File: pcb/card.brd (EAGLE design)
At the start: 69.5 x 40.6 mm, 24 parts, among them IC1 74HC14D, IC2 24LC256SN, Q1 BC817

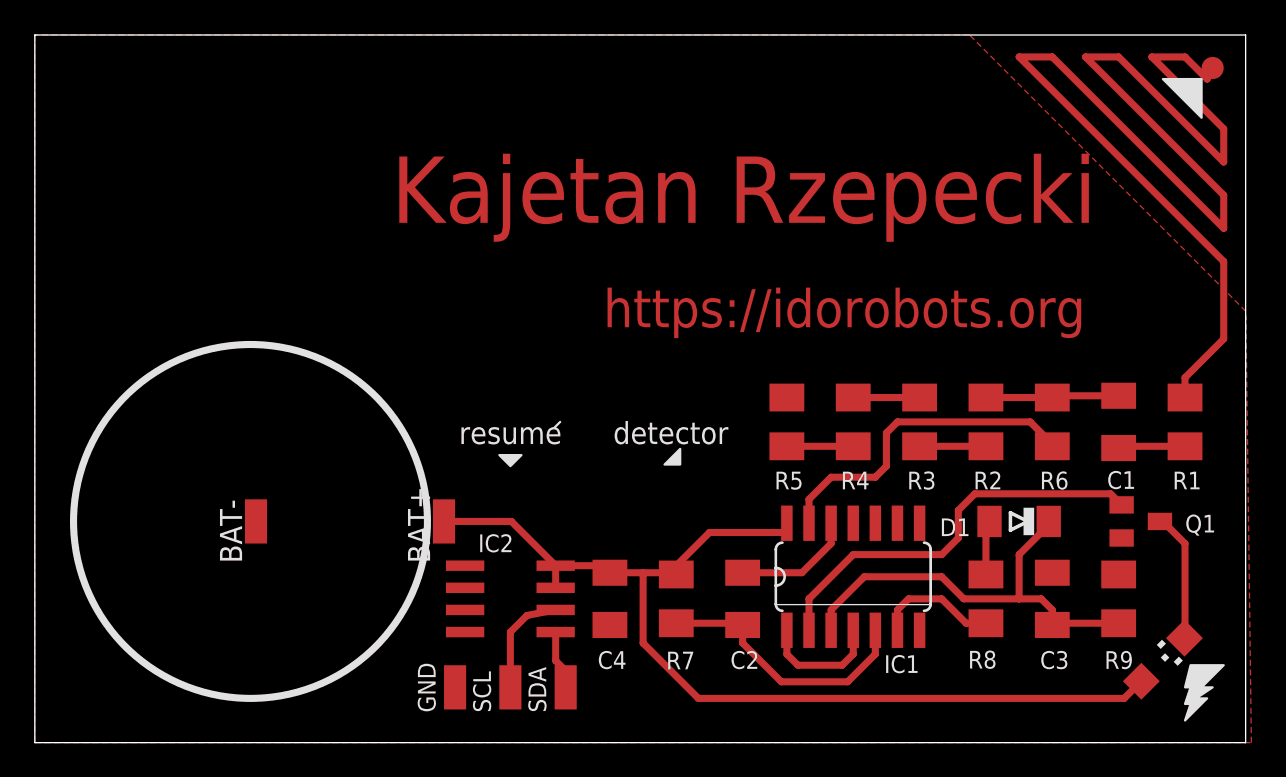
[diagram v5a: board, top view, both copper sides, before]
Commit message: Added the battery holder to the schematic.
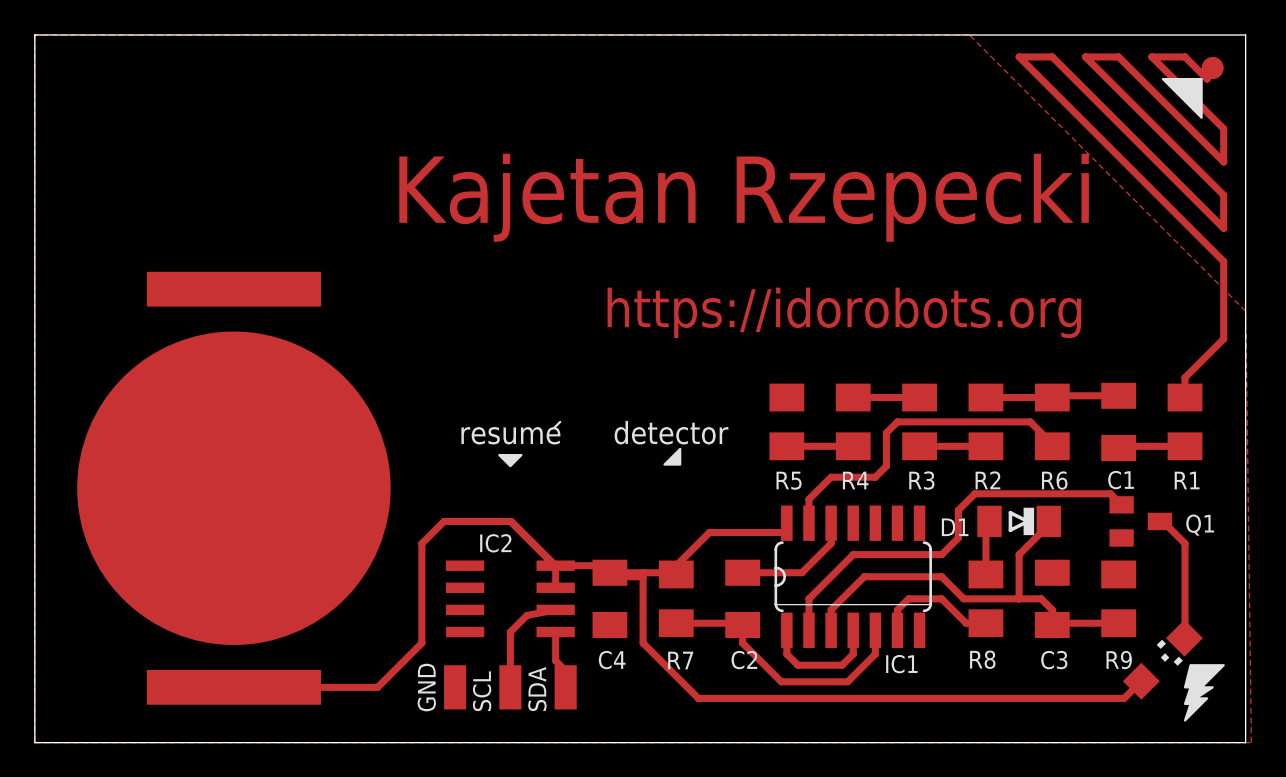
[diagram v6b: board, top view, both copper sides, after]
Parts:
- removed BAT+, BAT-: (no value), wirepad:SMD1,27-2,54
- added BAT: KB3003, bat:KB3003
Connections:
- net GND: now also BAT.-; no longer BAT-.1
- net VCC: now also BAT.+@1, BAT.+@2; no longer BAT+.1
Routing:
- net VCC: track 58.9 -> 85.1 mm
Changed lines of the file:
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@@
 <text x="60.96" y="33.655" size="3.81" layer="1" rot="R180">Kajetan Rzepecki</text>
 <text x="60.325" y="26.035" size="2.1844" layer="1" rot="R180">https://idorobots.org</text>
-<circle x="12.3825" y="12.7" radius="10.16" width="0.4064" layer="25"/>
 <text x="60.96" y="33.655" size="3.81" layer="29" rot="R180">Kajetan Rzepecki</text>
 <text x="60.325" y="26.035" size="2.1844" layer="29" rot="R180">https://idorobots.org</text>
@@
 <attribute name="NAME" x="26.1875" y="1.7275" size="1.016" layer="25" rot="R90"/>
 </element>
-<element name="BAT+" library="wirepad" package="SMD1,27-2,54" value="" x="23.495" y="12.7"/>
-<element name="BAT-" library="wirepad" package="SMD1,27-2,54" value="" x="12.7" y="12.7"/>
 <element name="IC2" library="microchip" package="SO-08" value="24LC256SN" x="27.305" y="8.255" smashed="yes" rot="R270">
 <attribute name="OC_FARNELL" value="9757996" x="27.305" y="8.255" size="1.016" layer="27" rot="R270" display="off"/>
@@
 <attribute name="VALUE" x="66.9925" y="37.973" size="0.0254" layer="27"/>
 </element>
+<element name="BAT" library="bat" package="KB3003" value="KB3003" x="11.43" y="14.605" rot="R90"/>
 </elements>
 <signals>
@@
 <vertex x="53.6575" y="40.64"/>
 </polygon>
-<contactref element="BAT-" pad="1"/>
 <contactref element="IC2" pad="1"/>
 <contactref element="IC2" pad="2"/>
@@
 <contactref element="GND" pad="1"/>
 <contactref element="R5" pad="1"/>
+<contactref element="BAT" pad="-"/>
 </signal>
 <signal name="VCC">
@@
 <contactref element="LED" pad="A"/>
 <contactref element="C4" pad="2"/>
-<contactref element="BAT+" pad="1"/>
 <contactref element="IC2" pad="8"/>
 <contactref element="IC2" pad="7"/>
@@
 <wire x1="38.735" y1="12.065" x2="43.18" y2="12.065" width="0.4064" layer="1"/>
 <wire x1="43.18" y1="12.065" x2="43.18" y2="12.5984" width="0.4064" layer="1"/>
-<wire x1="38.1" y1="2.54" x2="34.925" y2="5.715" width="0.4064" layer="1"/>
-<wire x1="34.925" y1="5.715" x2="34.925" y2="9.755" width="0.4064" layer="1"/>
+<wire x1="34.925" y1="9.525" x2="34.925" y2="9.755" width="0.4064" layer="1"/>
 <wire x1="29.905" y1="10.16" x2="29.905" y2="8.89" width="0.4064" layer="1"/>
 <wire x1="33.2775" y1="10.0125" x2="33.02" y2="9.755" width="0.4064" layer="1"/>
-<wire x1="23.495" y1="12.7" x2="27.365" y2="12.7" width="0.4064" layer="1"/>
 <wire x1="27.365" y1="12.7" x2="29.905" y2="10.16" width="0.4064" layer="1"/>
-<wire x1="29.905" y1="10.16" x2="32.9325" y2="10.16" width="0.4064" layer="1"/>
+<wire x1="29.905" y1="10.16" x2="32.385" y2="10.16" width="0.4064" layer="1"/>
+<wire x1="32.385" y1="10.16" x2="32.9325" y2="10.16" width="0.4064" layer="1"/>
 <wire x1="32.9325" y1="10.16" x2="33.02" y2="9.755" width="0.4064" layer="1"/>
+<contactref element="BAT" pad="+@2" route="any" routetag="G$1.+"/>
+<contactref element="BAT" pad="+@1" route="any" routetag="G$1.+"/>
+<wire x1="38.1" y1="2.54" x2="34.925" y2="5.715" width="0.4064" layer="1"/>
+<wire x1="34.925" y1="5.715" x2="34.925" y2="9.525" width="0.4064" layer="1"/>
+<wire x1="34.925" y1="9.525" x2="32.385" y2="9.525" width="0.4064" layer="1"/>
+<wire x1="32.385" y1="9.525" x2="32.385" y2="10.16" width="0.4064" layer="1"/>
+<wire x1="29.905" y1="10.16" x2="29.845" y2="10.16" width="0.4064" layer="1"/>
+<wire x1="29.845" y1="10.16" x2="27.305" y2="12.7" width="0.4064" layer="1"/>
+<wire x1="27.305" y1="12.7" x2="23.495" y2="12.7" width="0.4064" layer="1"/>
+<wire x1="23.495" y1="12.7" x2="22.225" y2="11.43" width="0.4064" layer="1"/>
+<wire x1="22.225" y1="11.43" x2="22.225" y2="5.715" width="0.4064" layer="1"/>
+<wire x1="22.225" y1="5.715" x2="19.685" y2="3.175" width="0.4064" layer="1"/>
+<wire x1="19.685" y1="3.175" x2="11.43" y2="3.175" width="0.4064" layer="1"/>
 </signal>
 <signal name="N$2">
